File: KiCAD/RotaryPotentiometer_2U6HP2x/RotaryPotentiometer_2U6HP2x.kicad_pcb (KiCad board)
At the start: 2 copper layers, 30 x 84 mm, 8 parts, among them J1 Conn_01x03_Socket, J2 Conn_01x03_Socket

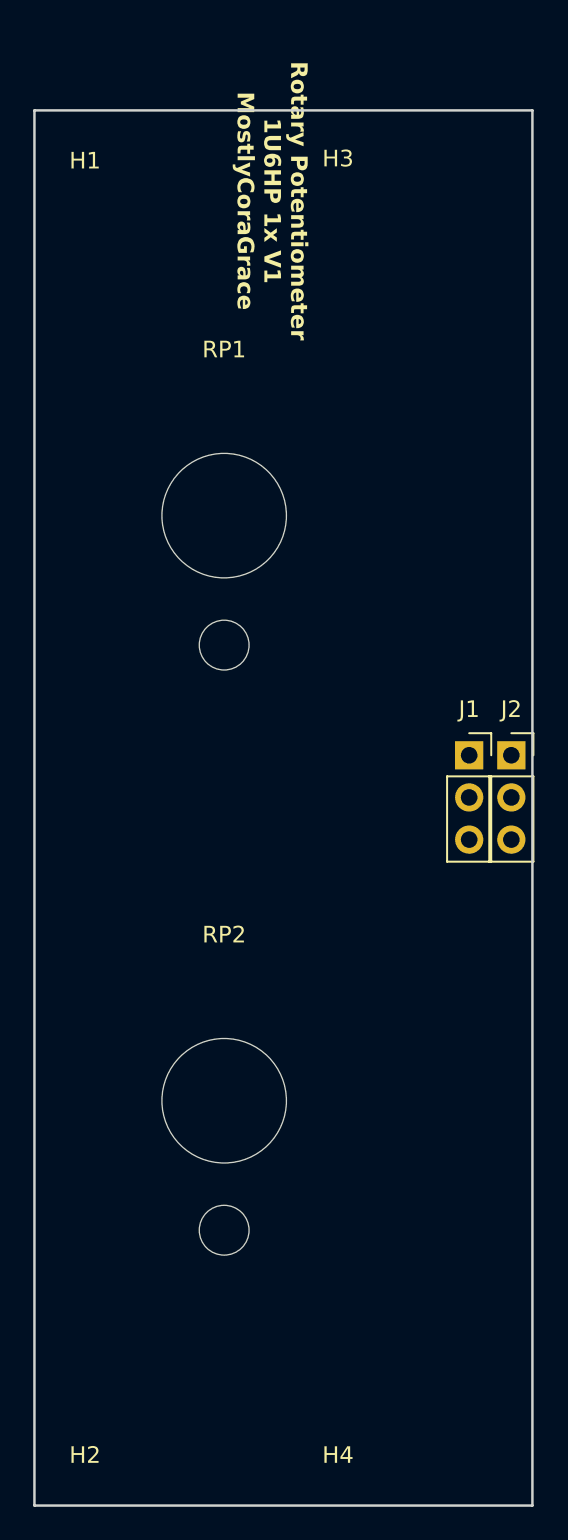
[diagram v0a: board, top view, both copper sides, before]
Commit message: removed all front silkscreen, and flipped most modules, to make the boards 'cleaner'.
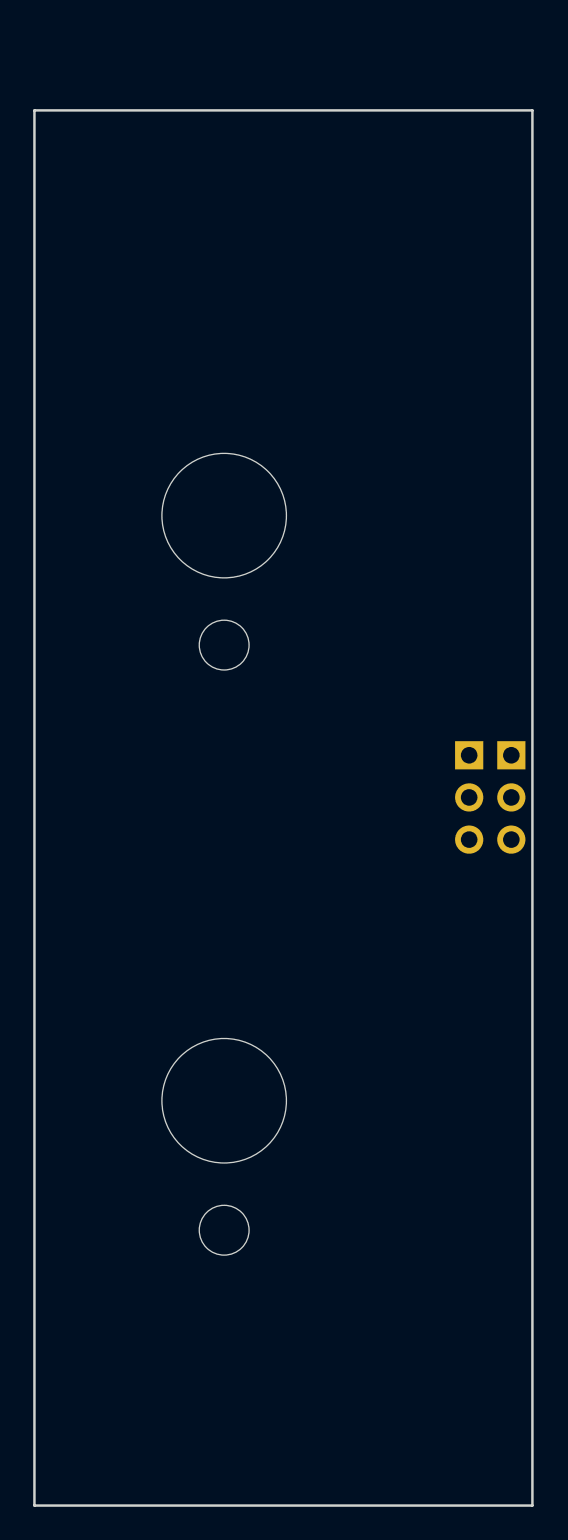
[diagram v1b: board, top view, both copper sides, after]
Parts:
- H1, H2, H3, H4, J1, J2: moved to B.Cu
- turned H1 to 180 degrees
- turned H2 to 180 degrees
- turned H3 to 180 degrees
- turned H4 to 180 degrees
- turned J1 to 180 degrees
- turned J2 to 180 degrees

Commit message: added copper fills to every module, to maybe possibly increase structural rigidity.
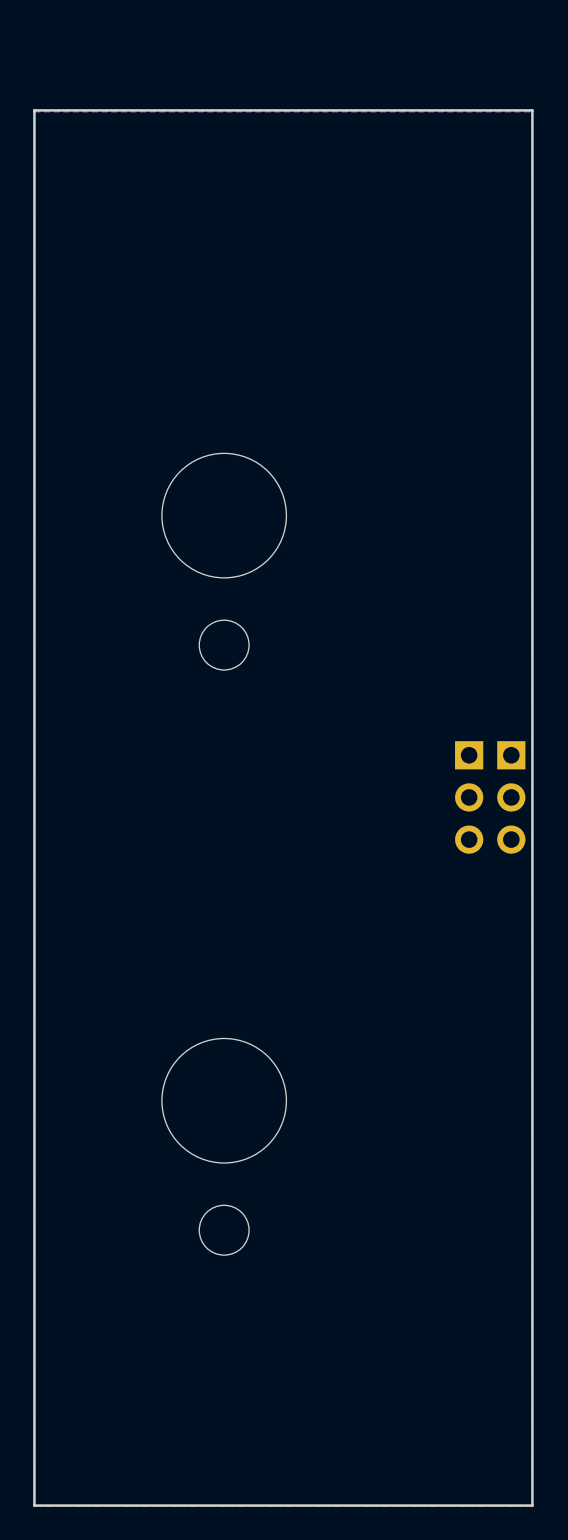
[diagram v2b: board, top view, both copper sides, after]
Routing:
- added copper zone on B.Cu, net (none)
- added copper zone on F.Cu, net (none)
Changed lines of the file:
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@@
 		(at 11.43 26.8375)
 		(property "Reference" "RP1"
-			(at 0 -10 -0)
+			(at 0 -10 0)
 			(unlocked yes)
 			(layer "B.SilkS")
@@
 		)
 		(fp_text user "${REFERENCE}"
-			(at 0 -10 -0)
+			(at 0 -10 0)
 			(unlocked yes)
 			(layer "B.Fab")
@@
 		(at 11.43 62.0875)
 		(property "Reference" "RP2"
-			(at 0 -10 -0)
+			(at 0 -10 0)
 			(unlocked yes)
 			(layer "B.SilkS")
@@
 		)
 		(fp_text user "${REFERENCE}"
-			(at 0 -10 -0)
+			(at 0 -10 0)
 			(unlocked yes)
 			(layer "B.Fab")
@@
 		)
 	)
+	(zone
+		(net 0)
+		(net_name "")
+		(layers "F&B.Cu")
+		(hatch edge 0.5)
+		(connect_pads
+			(clearance 0.5)
+		)
+		(min_thickness 0.25)
+		(filled_areas_thickness no)
+		(fill yes
+			(thermal_gap 0.5)
+			(thermal_bridge_width 0.5)
+			(island_removal_mode 1)
+			(island_area_min 10)
+		)
+		(polygon
+			(pts
+				(xy 0 2.5) (xy 30 2.5) (xy 30 86.5) (xy 0 86.5)
+			)
+		)
+	)
